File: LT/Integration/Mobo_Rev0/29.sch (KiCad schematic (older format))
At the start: 12 parts

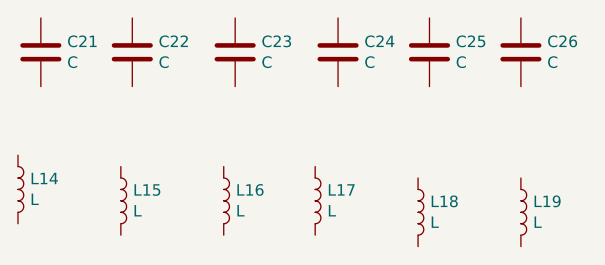
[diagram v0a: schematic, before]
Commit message: I uploaded the schematics for the receiving stage into their respective hierarchial sheets and have begun the integration of the received stage
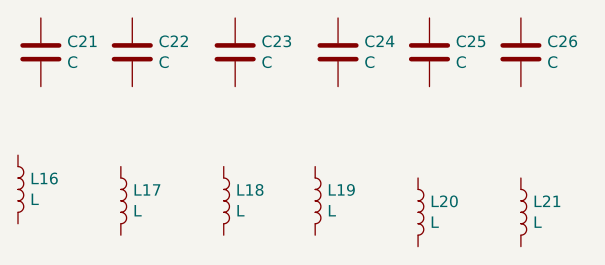
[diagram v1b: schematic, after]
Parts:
- C21, C22, C23, C24, C25, C26: footprint Capacitor_SMD:C_0805_2012Metric -> (none)
- L16: renamed from L14; footprint Inductor_SMD:L_0805_2012Metric -> (none)
- L17: renamed from L15; footprint Inductor_SMD:L_0805_2012Metric -> (none)
- L18: renamed from L16; footprint Inductor_SMD:L_0805_2012Metric -> (none)
- L19: renamed from L17; footprint Inductor_SMD:L_0805_2012Metric -> (none)
- L20: renamed from L18; footprint Inductor_SMD:L_0805_2012Metric -> (none)
- L21: renamed from L19; footprint Inductor_SMD:L_0805_2012Metric -> (none)
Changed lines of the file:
@@
 F 0 "C21" H 2215 1496 50  0000 L CNN
 F 1 "C" H 2215 1405 50  0000 L CNN
-F 2 "Capacitor_SMD:C_0805_2012Metric" H 2138 1300 50  0001 C CNN
+F 2 "" H 2138 1300 50  0001 C CNN
 F 3 "~" H 2100 1450 50  0001 C CNN
 	1    2100 1450
@@
 F 0 "C22" H 2615 1496 50  0000 L CNN
 F 1 "C" H 2615 1405 50  0000 L CNN
-F 2 "Capacitor_SMD:C_0805_2012Metric" H 2538 1300 50  0001 C CNN
+F 2 "" H 2538 1300 50  0001 C CNN
 F 3 "~" H 2500 1450 50  0001 C CNN
 	1    2500 1450
@@
 F 0 "C23" H 3065 1496 50  0000 L CNN
 F 1 "C" H 3065 1405 50  0000 L CNN
-F 2 "Capacitor_SMD:C_0805_2012Metric" H 2988 1300 50  0001 C CNN
+F 2 "" H 2988 1300 50  0001 C CNN
 F 3 "~" H 2950 1450 50  0001 C CNN
 	1    2950 1450
@@
 F 0 "C24" H 3515 1496 50  0000 L CNN
 F 1 "C" H 3515 1405 50  0000 L CNN
-F 2 "Capacitor_SMD:C_0805_2012Metric" H 3438 1300 50  0001 C CNN
+F 2 "" H 3438 1300 50  0001 C CNN
 F 3 "~" H 3400 1450 50  0001 C CNN
 	1    3400 1450
@@
 F 0 "C25" H 3915 1496 50  0000 L CNN
 F 1 "C" H 3915 1405 50  0000 L CNN
-F 2 "Capacitor_SMD:C_0805_2012Metric" H 3838 1300 50  0001 C CNN
+F 2 "" H 3838 1300 50  0001 C CNN
 F 3 "~" H 3800 1450 50  0001 C CNN
 	1    3800 1450
@@
 F 0 "C26" H 4315 1496 50  0000 L CNN
 F 1 "C" H 4315 1405 50  0000 L CNN
-F 2 "Capacitor_SMD:C_0805_2012Metric" H 4238 1300 50  0001 C CNN
+F 2 "" H 4238 1300 50  0001 C CNN
 F 3 "~" H 4200 1450 50  0001 C CNN
 	1    4200 1450
@@
 $EndComp
 $Comp
-L Device:L L14
+L Device:L L16
 U 1 1 5E4B344D
 P 2000 2050
-F 0 "L14" H 2053 2096 50  0000 L CNN
+F 0 "L16" H 2053 2096 50  0000 L CNN
 F 1 "L" H 2053 2005 50  0000 L CNN
-F 2 "Inductor_SMD:L_0805_2012Metric" H 2000 2050 50  0001 C CNN
+F 2 "" H 2000 2050 50  0001 C CNN
 F 3 "~" H 2000 2050 50  0001 C CNN
 	1    2000 2050
@@
 $EndComp
 $Comp
-L Device:L L15
+L Device:L L17
 U 1 1 5E4B34CB
 P 2450 2100
-F 0 "L15" H 2503 2146 50  0000 L CNN
+F 0 "L17" H 2503 2146 50  0000 L CNN
 F 1 "L" H 2503 2055 50  0000 L CNN
-F 2 "Inductor_SMD:L_0805_2012Metric" H 2450 2100 50  0001 C CNN
+F 2 "" H 2450 2100 50  0001 C CNN
 F 3 "~" H 2450 2100 50  0001 C CNN
 	1    2450 2100
@@
 $EndComp
 $Comp
-L Device:L L16
+L Device:L L18
 U 1 1 5E4B3518
 P 2900 2100
-F 0 "L16" H 2953 2146 50  0000 L CNN
+F 0 "L18" H 2953 2146 50  0000 L CNN
 F 1 "L" H 2953 2055 50  0000 L CNN
-F 2 "Inductor_SMD:L_0805_2012Metric" H 2900 2100 50  0001 C CNN
+F 2 "" H 2900 2100 50  0001 C CNN
 F 3 "~" H 2900 2100 50  0001 C CNN
 	1    2900 2100
@@
 $EndComp
 $Comp
-L Device:L L17
+L Device:L L19
 U 1 1 5E4B35FA
 P 3300 2100
-F 0 "L17" H 3353 2146 50  0000 L CNN
+F 0 "L19" H 3353 2146 50  0000 L CNN
 F 1 "L" H 3353 2055 50  0000 L CNN
-F 2 "Inductor_SMD:L_0805_2012Metric" H 3300 2100 50  0001 C CNN
+F 2 "" H 3300 2100 50  0001 C CNN
 F 3 "~" H 3300 2100 50  0001 C CNN
 	1    3300 2100
@@
 $EndComp
 $Comp
-L Device:L L18
+L Device:L L20
 U 1 1 5E4B3601
 P 3750 2150
-F 0 "L18" H 3803 2196 50  0000 L CNN
+F 0 "L20" H 3803 2196 50  0000 L CNN
 F 1 "L" H 3803 2105 50  0000 L CNN
-F 2 "Inductor_SMD:L_0805_2012Metric" H 3750 2150 50  0001 C CNN
+F 2 "" H 3750 2150 50  0001 C CNN
 F 3 "~" H 3750 2150 50  0001 C CNN
 	1    3750 2150
@@
 $EndComp
 $Comp
-L Device:L L19
+L Device:L L21
 U 1 1 5E4B3608
 P 4200 2150
-F 0 "L19" H 4253 2196 50  0000 L CNN
+F 0 "L21" H 4253 2196 50  0000 L CNN
 F 1 "L" H 4253 2105 50  0000 L CNN
-F 2 "Inductor_SMD:L_0805_2012Metric" H 4200 2150 50  0001 C CNN
+F 2 "" H 4200 2150 50  0001 C CNN
 F 3 "~" H 4200 2150 50  0001 C CNN
 	1    4200 2150

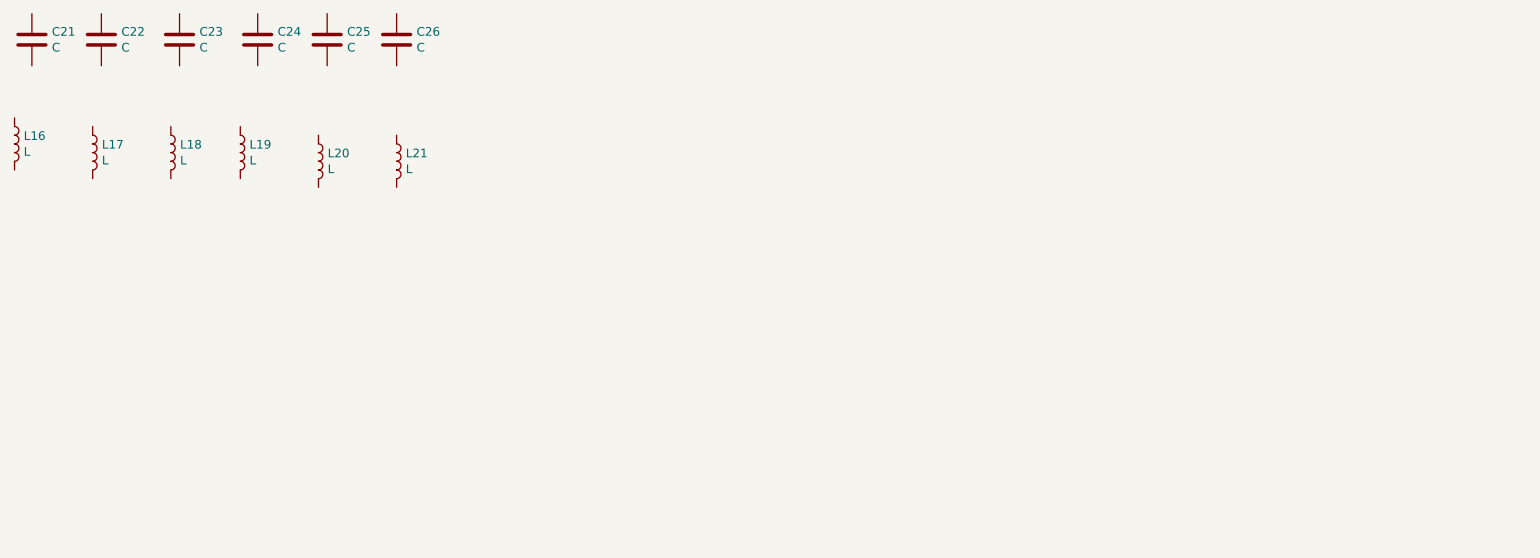
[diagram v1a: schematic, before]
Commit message: Finished a preliminary layout for the Receiving Stage, and uploaded the schematics for the Pre-Amp, 29.4 BPF, and 29.4 LPF.
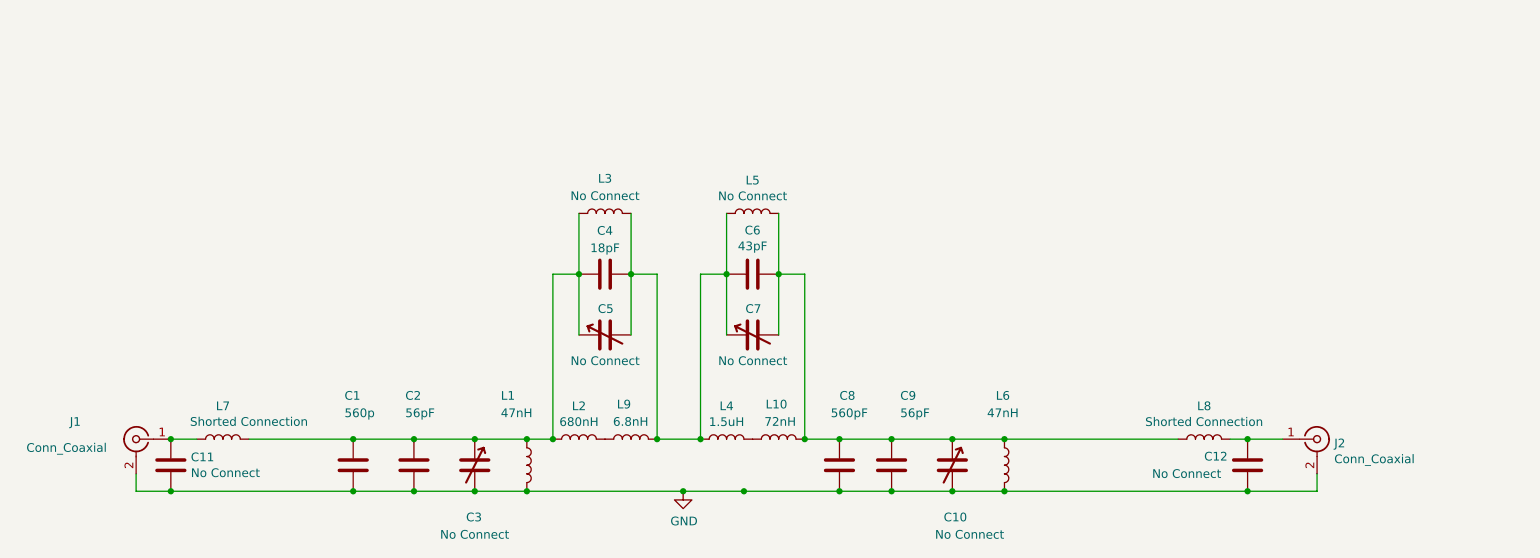
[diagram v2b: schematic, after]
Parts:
- removed C21, C22, C23, C24, C25, C26: C, symbol Device:C
- removed L16, L17, L18, L19, L20, L21: L, symbol Device:L
- added C1: 560p, Capacitor_SMD:C_0805_2012Metric_Pad1.15x1.40mm_HandSolder, symbol Device:C
- added C10, C3, C5, C7: No Connect, Connector_PinHeader_2.54mm:Variable Capacitor, symbol Device:C_Variable
- added C11, C12: No Connect, Capacitor_SMD:C_0805_2012Metric_Pad1.15x1.40mm_HandSolder, symbol Device:C
- added C2, C9: 56pF, Capacitor_SMD:C_0805_2012Metric_Pad1.15x1.40mm_HandSolder, symbol Device:C
- added C4: 18pF, Capacitor_SMD:C_0805_2012Metric_Pad1.15x1.40mm_HandSolder, symbol Device:C
- added C6: 43pF, Capacitor_SMD:C_0805_2012Metric_Pad1.15x1.40mm_HandSolder, symbol Device:C
- added C8: 560pF, Capacitor_SMD:C_0805_2012Metric_Pad1.15x1.40mm_HandSolder, symbol Device:C
- added J1, J2: Conn_Coaxial, Connector_Coaxial:SMA_Amphenol_132289_EdgeMount, symbol Connector:Conn_Coaxial
- added L1, L6: 47nH, Inductor_SMD:L_0805_2012Metric_Pad1.15x1.40mm_HandSolder, symbol Device:L
- added L10: 72nH, Inductor_SMD:L_0805_2012Metric_Pad1.15x1.40mm_HandSolder, symbol Device:L
- added L2: 680nH, Inductor_SMD:L_0805_2012Metric_Pad1.15x1.40mm_HandSolder, symbol Device:L
- added L3, L5: No Connect, Inductor_SMD:L_0805_2012Metric_Pad1.15x1.40mm_HandSolder, symbol Device:L
- added L4: 1.5uH, Inductor_SMD:L_0805_2012Metric_Pad1.15x1.40mm_HandSolder, symbol Device:L
- added L7, L8: Shorted Connection, Inductor_SMD:L_0805_2012Metric_Pad1.15x1.40mm_HandSolder, symbol Device:L
- added L9: 6.8nH, Inductor_SMD:L_0805_2012Metric_Pad1.15x1.40mm_HandSolder, symbol Device:L
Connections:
- new net: C1.1, C2.1, C3.1, C4.2, C5.1, L1.1, L2.1, L3.1, L7.2
- new net: C4.1, C5.2, C6.2, C7.1, L3.2, L4.1, L5.1, L9.2
- new net: C10.1, C6.1, C7.2, C8.1, C9.1, L10.2, L5.2, L6.1, L8.1
- new net: L10.1, L4.2
- new net: L2.2, L9.1
- new net: C12.1, J2.1 (In), L8.2
- new net: C11.1, J1.1 (In), L7.1
- new net GND: C1.2, C10.2, C11.2, C12.2, C2.2, C3.2, C8.2, C9.2, J1.2 (Ext), J2.2 (Ext), L1.2, L6.2

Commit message: Uploaded Schematics to Integration of Phase 2
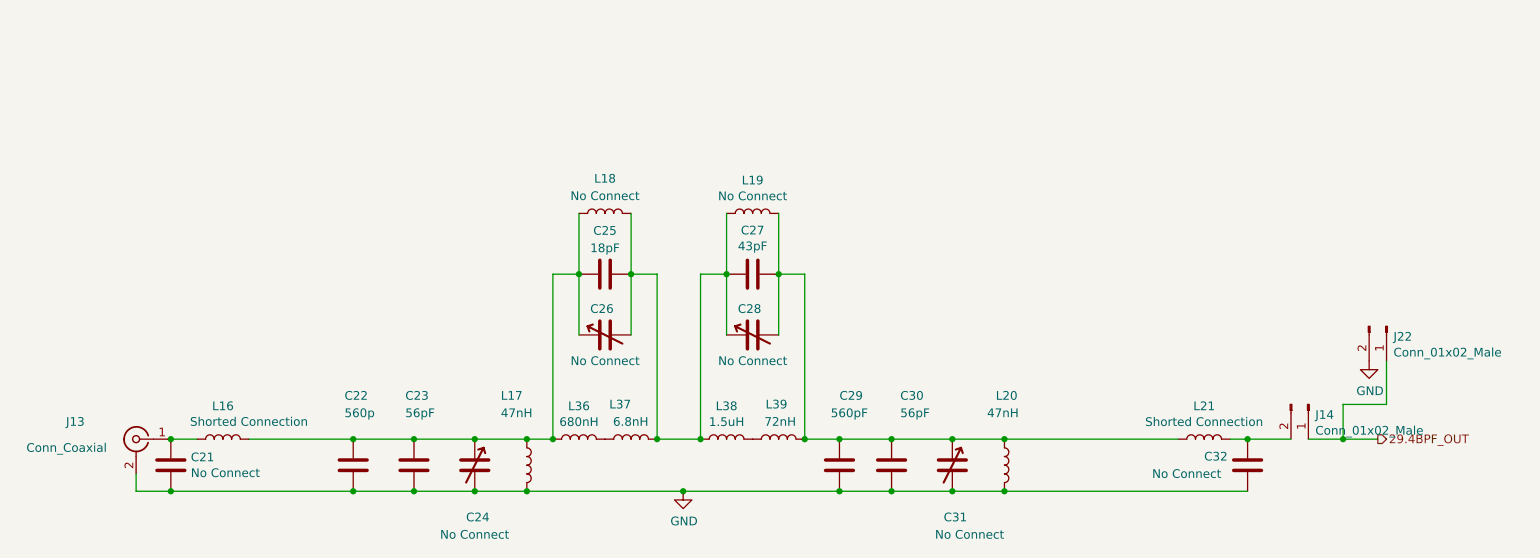
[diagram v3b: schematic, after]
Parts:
- removed J2: Conn_Coaxial, Connector_Coaxial:SMA_Amphenol_132289_EdgeMount, symbol Connector:Conn_Coaxial
- added J14: Conn_01x02_Male, Connector_PinHeader_2.54mm:PinHeader_1x02_P2.54mm_Vertical, symbol Connector:Conn_01x02_Male
- added J22: Conn_01x02_Male, Connector_Coaxial:SMA_Amphenol_132289_EdgeMount, symbol Connector:Conn_01x02_Male
- renumbered C11 to C21, C1 to C22, C2 to C23, C3 to C24, C4 to C25, C5 to C26, C6 to C27, C7 to C28, C8 to C29, C9 to C30, C10 to C31, C12 to C32, J1 to J13, L7 to L16, L1 to L17, L3 to L18, L5 to L19, L6 to L20, L8 to L21, L2 to L36, L9 to L37, L4 to L38, L10 to L39
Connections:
- net GND: now also J22.2 (Pin_2)
- net at C32.1, L21.2: now also J14.2 (Pin_2)
- new net 29.4BPF_OUT: J14.1 (Pin_1), J22.1 (Pin_1)
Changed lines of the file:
@@
 EESchema Schematic File Version 4
-LIBS:3rd Order Inverse Chebyshev-cache
+LIBS:Mobo_Rev1-cache
 EELAYER 26 0
 EELAYER END
 $Descr A4 11693 8268
 encoding utf-8
-Sheet 1 1
+Sheet 6 10
 Title ""
 Date ""
@@
 $EndDescr
 $Comp
-L Device:C C1
+L Device:C C22
 U 1 1 5E276963
 P 3950 3900
-F 0 "C1" H 3900 4300 50  0000 L CNN
+F 0 "C22" H 3900 4300 50  0000 L CNN
 F 1 "560p" H 3900 4200 50  0000 L CNN
 F 2 "Capacitor_SMD:C_0805_2012Metric_Pad1.15x1.40mm_HandSolder" H 3988 3750 50  0001 C CNN
@@
 $EndComp
 $Comp
-L Device:C C2
+L Device:C C23
 U 1 1 5E27699C
 P 4300 3900
-F 0 "C2" H 4250 4300 50  0000 L CNN
+F 0 "C23" H 4250 4300 50  0000 L CNN
 F 1 "56pF" H 4250 4200 50  0000 L CNN
 F 2 "Capacitor_SMD:C_0805_2012Metric_Pad1.15x1.40mm_HandSolder" H 4338 3750 50  0001 C CNN
@@
 $EndComp
 $Comp
-L Device:C_Variable C3
+L Device:C_Variable C24
 U 1 1 5E2769F8
 P 4650 3900
-F 0 "C3" H 4600 3600 50  0000 L CNN
+F 0 "C24" H 4600 3600 50  0000 L CNN
 F 1 "No Connect" H 4450 3500 50  0000 L CNN
 F 2 "Connector_PinHeader_2.54mm:Variable Capacitor" H 4650 3900 50  0001 C CNN
@@
 $EndComp
 $Comp
-L Device:L L1
+L Device:L L17
 U 1 1 5E276A4B
 P 4950 3900
-F 0 "L1" H 4800 4300 50  0000 L CNN
+F 0 "L17" H 4800 4300 50  0000 L CNN
 F 1 "47nH" H 4800 4200 50  0000 L CNN
 F 2 "Inductor_SMD:L_0805_2012Metric_Pad1.15x1.40mm_HandSolder" H 4950 3900 50  0001 C CNN
@@
 $EndComp
 $Comp
-L Device:L L3
+L Device:L L18
 U 1 1 5E276AB0
 P 5400 2450
-F 0 "L3" V 5600 2450 50  0000 C CNN
+F 0 "L18" V 5600 2450 50  0000 C CNN
 F 1 "No Connect" V 5500 2450 50  0000 C CNN
 F 2 "Inductor_SMD:L_0805_2012Metric_Pad1.15x1.40mm_HandSolder" H 5400 2450 50  0001 C CNN
@@
 $EndComp
 $Comp
-L Device:C C8
+L Device:C C29
 U 1 1 5E276BA2
 P 6750 3900
-F 0 "C8" H 6750 4300 50  0000 L CNN
+F 0 "C29" H 6750 4300 50  0000 L CNN
 F 1 "560pF" H 6700 4200 50  0000 L CNN
 F 2 "Capacitor_SMD:C_0805_2012Metric_Pad1.15x1.40mm_HandSolder" H 6788 3750 50  0001 C CNN
@@
 $EndComp
 $Comp
-L Device:C C9
+L Device:C C30
 U 1 1 5E276BEC
 P 7050 3900
-F 0 "C9" H 7100 4300 50  0000 L CNN
+F 0 "C30" H 7100 4300 50  0000 L CNN
 F 1 "56pF" H 7100 4200 50  0000 L CNN
 F 2 "Capacitor_SMD:C_0805_2012Metric_Pad1.15x1.40mm_HandSolder" H 7088 3750 50  0001 C CNN
@@
 $EndComp
 $Comp
-L Device:C_Variable C10
+L Device:C_Variable C31
 U 1 1 5E276C50
 P 7400 3900
-F 0 "C10" H 7350 3600 50  0000 L CNN
+F 0 "C31" H 7350 3600 50  0000 L CNN
 F 1 "No Connect" H 7300 3500 50  0000 L CNN
 F 2 "Connector_PinHeader_2.54mm:Variable Capacitor" H 7400 3900 50  0001 C CNN
@@
 $EndComp
 $Comp
-L Device:L L6
+L Device:L L20
 U 1 1 5E276CB9
 P 7700 3900
-F 0 "L6" H 7650 4300 50  0000 L CNN
+F 0 "L20" H 7650 4300 50  0000 L CNN
 F 1 "47nH" H 7600 4200 50  0000 L CNN
 F 2 "Inductor_SMD:L_0805_2012Metric_Pad1.15x1.40mm_HandSolder" H 7700 3900 50  0001 C CNN
@@
 $EndComp
 $Comp
-L Device:L L5
+L Device:L L19
 U 1 1 5E276DA0
 P 6250 2450
-F 0 "L5" V 6440 2450 50  0000 C CNN
+F 0 "L19" V 6440 2450 50  0000 C CNN
 F 1 "No Connect" V 6349 2450 50  0000 C CNN
 F 2 "Inductor_SMD:L_0805_2012Metric_Pad1.15x1.40mm_HandSolder" H 6250 2450 50  0001 C CNN
@@
 $EndComp
 $Comp
-L Device:C C6
+L Device:C C27
 U 1 1 5E276E5D
 P 6250 2800
-F 0 "C6" V 5998 2800 50  0000 C CNN
+F 0 "C27" V 5998 2800 50  0000 C CNN
 F 1 "43pF" V 6089 2800 50  0000 C CNN
 F 2 "Capacitor_SMD:C_0805_2012Metric_Pad1.15x1.40mm_HandSolder" H 6288 2650 50  0001 C CNN
@@
 $EndComp
 $Comp
-L Device:C C4
+L Device:C C25
 U 1 1 5E276EEB
 P 5400 2800
-F 0 "C4" V 5150 2800 50  0000 C CNN
+F 0 "C25" V 5150 2800 50  0000 C CNN
 F 1 "18pF" V 5250 2800 50  0000 C CNN
 F 2 "Capacitor_SMD:C_0805_2012Metric_Pad1.15x1.40mm_HandSolder" H 5438 2650 50  0001 C CNN
@@
 $EndComp
 $Comp
-L Device:L L4
+L Device:L L38
 U 1 1 5E276F67
 P 6100 3750
-F 0 "L4" V 6290 3750 50  0000 C CNN
+F 0 "L38" V 6290 3750 50  0000 C CNN
 F 1 "1.5uH" V 6199 3750 50  0000 C CNN
 F 2 "Inductor_SMD:L_0805_2012Metric_Pad1.15x1.40mm_HandSolder" H 6100 3750 50  0001 C CNN
@@
 $EndComp
 $Comp
-L Device:L L2
+L Device:L L36
 U 1 1 5E277001
 P 5250 3750
-F 0 "L2" V 5440 3750 50  0000 C CNN
+F 0 "L36" V 5440 3750 50  0000 C CNN
 F 1 "680nH" V 5349 3750 50  0000 C CNN
 F 2 "Inductor_SMD:L_0805_2012Metric_Pad1.15x1.40mm_HandSolder" H 5250 3750 50  0001 C CNN
@@
 $EndComp
 $Comp
-L Device:C_Variable C5
+L Device:C_Variable C26
 U 1 1 5E2770B3
 P 5400 3150
-F 0 "C5" V 5550 3100 50  0000 L CNN
+F 0 "C26" V 5550 3100 50  0000 L CNN
 F 1 "No Connect" V 5250 2950 50  0000 L CNN
 F 2 "Connector_PinHeader_2.54mm:Variable Capacitor" H 5400 3150 50  0001 C CNN
@@
 $EndComp
 $Comp
-L Device:C_Variable C7
+L Device:C_Variable C28
 U 1 1 5E2772FD
 P 6250 3150
-F 0 "C7" V 6400 3100 50  0000 L CNN
+F 0 "C28" V 6400 3100 50  0000 L CNN
 F 1 "No Connect" V 6100 2950 50  0000 L CNN
 F 2 "Connector_PinHeader_2.54mm:Variable Capacitor" H 6250 3150 50  0001 C CNN
@@
 $EndComp
 $Comp
-L Connector:Conn_Coaxial J2
-U 1 1 5E27740C
-P 9500 3750
-F 0 "J2" H 9599 3726 50  0000 L CNN
-F 1 "Conn_Coaxial" H 9599 3635 50  0000 L CNN
-F 2 "Connector_Coaxial:SMA_Amphenol_132289_EdgeMount" H 9500 3750 50  0001 C CNN
-F 3 " ~" H 9500 3750 50  0001 C CNN
-	1    9500 3750
-	1    0    0    -1
-$EndComp
-$Comp
-L Connector:Conn_Coaxial J1
+L Connector:Conn_Coaxial J13
 U 1 1 5E2774D2
 P 2700 3750
-F 0 "J1" H 3050 3850 50  0000 C CNN
+F 0 "J13" H 3050 3850 50  0000 C CNN
 F 1 "Conn_Coaxial" H 3100 3700 50  0000 C CNN
 F 2 "Connector_Coaxial:SMA_Amphenol_132289_EdgeMount" H 2700 3750 50  0001 C CNN
@@
 Wire Wire Line
 	4650 3750 4950 3750
-Wire Wire Line
-	9300 3750 9100 3750
 Connection ~ 7050 3750
 Wire Wire Line
@@
 	2700 4050 2900 4050
 Wire Wire Line
-	9500 4050 9500 3950
-Wire Wire Line
 	3950 4050 4300 4050
 Connection ~ 4300 4050
@@
 	7400 4050 7700 4050
 $Comp
-L power:GND #PWR0101
+L power:GND #PWR0108
 U 1 1 5E277AE7
 P 5850 4050
-F 0 "#PWR0101" H 5850 3800 50  0001 C CNN
+F 0 "#PWR0108" H 5850 3800 50  0001 C CNN
 F 1 "GND" H 5855 3877 50  0000 C CNN
 F 2 "" H 5850 4050 50  0001 C CNN
@@
 	1    0    0    -1
 $EndComp
-Connection ~ 6200 4050
-Wire Wire Line
-	6200 4050 6750 4050
-$Comp
-L Device:L L7
+$Comp
+L Device:L L16
 U 1 1 5E2812E7
 P 3200 3750
-F 0 "L7" V 3390 3750 50  0000 C CNN
+F 0 "L16" V 3390 3750 50  0000 C CNN
 F 1 "Shorted Connection" V 3300 3600 50  0000 C CNN
 F 2 "Inductor_SMD:L_0805_2012Metric_Pad1.15x1.40mm_HandSolder" H 3200 3750 50  0001 C CNN
@@
 $EndComp
 $Comp
-L Device:C C11
+L Device:C C21
 U 1 1 5E28138E
 P 2900 3900
-F 0 "C11" H 3015 3946 50  0000 L CNN
+F 0 "C21" H 3015 3946 50  0000 L CNN
 F 1 "No Connect" H 3015 3855 50  0000 L CNN
 F 2 "Capacitor_SMD:C_0805_2012Metric_Pad1.15x1.40mm_HandSolder" H 2938 3750 50  0001 C CNN
@@
 Connection ~ 3950 4050
 $Comp
-L Device:C C12
+L Device:C C32
 U 1 1 5E283E7E
 P 9100 3900
-F 0 "C12" H 8850 3950 50  0000 L CNN
+F 0 "C32" H 8850 3950 50  0000 L CNN
 F 1 "No Connect" H 8550 3850 50  0000 L CNN
 F 2 "Capacitor_SMD:C_0805_2012Metric_Pad1.15x1.40mm_HandSolder" H 9138 3750 50  0001 C CNN
@@
 $EndComp
 $Comp
-L Device:L L8
+L Device:L L21
 U 1 1 5E283F21
 P 8850 3750
-F 0 "L8" V 9040 3750 50  0000 C CNN
+F 0 "L21" V 9040 3750 50  0000 C CNN
 F 1 "Shorted Connection" V 8949 3750 50  0000 C CNN
 F 2 "Inductor_SMD:L_0805_2012Metric_Pad1.15x1.40mm_HandSolder" H 8850 3750 50  0001 C CNN
@@
 	2900 4050 3950 4050
 Wire Wire Line
-	9100 4050 9500 4050
-Connection ~ 9100 3750
-Wire Wire Line
 	9100 3750 9000 3750
 Connection ~ 2900 3750
@@
 Connection ~ 3950 3750
 $Comp
-L Device:L L9
+L Device:L L37
 U 1 1 5E3795A2
 P 5550 3750
-F 0 "L9" V 5750 3750 50  0000 L CNN
+F 0 "L37" V 5750 3750 50  0000 L CNN
 F 1 "6.8nH" V 5650 3650 50  0000 L CNN
 F 2 "Inductor_SMD:L_0805_2012Metric_Pad1.15x1.40mm_HandSolder" H 5550 3750 50  0001 C CNN
@@
 $EndComp
 $Comp
-L Device:L L10
+L Device:L L39
 U 1 1 5E379632
 P 6400 3750
-F 0 "L10" V 6600 3700 50  0000 L CNN
+F 0 "L39" V 6600 3700 50  0000 L CNN
 F 1 "72nH" V 6500 3650 50  0000 L CNN
 F 2 "Inductor_SMD:L_0805_2012Metric_Pad1.15x1.40mm_HandSolder" H 6400 3750 50  0001 C CNN
@@
 	7700 4050 9100 4050
 Connection ~ 7700 4050
-Connection ~ 9100 4050
 Connection ~ 5850 4050
 Wire Wire Line
-	5850 4050 6200 4050
+	5850 4050 6750 4050
+Text HLabel 9850 3750 2    50   Output ~ 0
+29.4BPF_OUT
+Wire Wire Line
+	9850 3750 9650 3750
+$Comp
+L Connector:Conn_01x02_Male J14
+U 1 1 5EA00F7C
+P 9450 3550
+F 0 "J14" V 9510 3590 50  0000 L CNN
+F 1 "Conn_01x02_Male" V 9601 3590 50  0000 L CNN
+F 2 "Connector_PinHeader_2.54mm:PinHeader_1x02_P2.54mm_Vertical" H 9450 3550 50  0001 C CNN
+F 3 "~" H 9450 3550 50  0001 C CNN
+	1    9450 3550
+	0    1    1    0
+$EndComp
+Wire Wire Line
+	9100 3750 9350 3750
+Connection ~ 9100 3750
+$Comp
+L Connector:Conn_01x02_Male J22
+U 1 1 5E9FC4D5
+P 9900 3100
+F 0 "J22" V 9960 3140 50  0000 L CNN
+F 1 "Conn_01x02_Male" V 10051 3140 50  0000 L CNN
+F 2 "Connector_Coaxial:SMA_Amphenol_132289_EdgeMount" H 9900 3100 50  0001 C CNN
+F 3 "~" H 9900 3100 50  0001 C CNN
+	1    9900 3100
+	0    1    1    0
+$EndComp
+$Comp
+L power:GND #PWR0102
+U 1 1 5E9FC7DA
+P 9800 3300
+F 0 "#PWR0102" H 9800 3050 50  0001 C CNN
+F 1 "GND" H 9805 3127 50  0000 C CNN
+F 2 "" H 9800 3300 50  0001 C CNN
+F 3 "" H 9800 3300 50  0001 C CNN
+	1    9800 3300
+	1    0    0    -1
+$EndComp
+Wire Wire Line
+	9900 3300 9900 3550
+Wire Wire Line
+	9900 3550 9650 3550
+Wire Wire Line
+	9650 3550 9650 3750
+Connection ~ 9650 3750
+Wire Wire Line
+	9650 3750 9450 3750
 $EndSCHEMATC
